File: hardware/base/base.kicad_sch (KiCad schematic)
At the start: 40 parts, among them J1 SWD, J2 USB_B_Mini, J4 Serial Interface, J5 Debug, Q1 Q_NMOS_GSD, SW3 RotaryEncoder_Switch, U1 nRF52833-QDxx, U2 Linear regulator, Y1 32MHz, Y2 32kHz

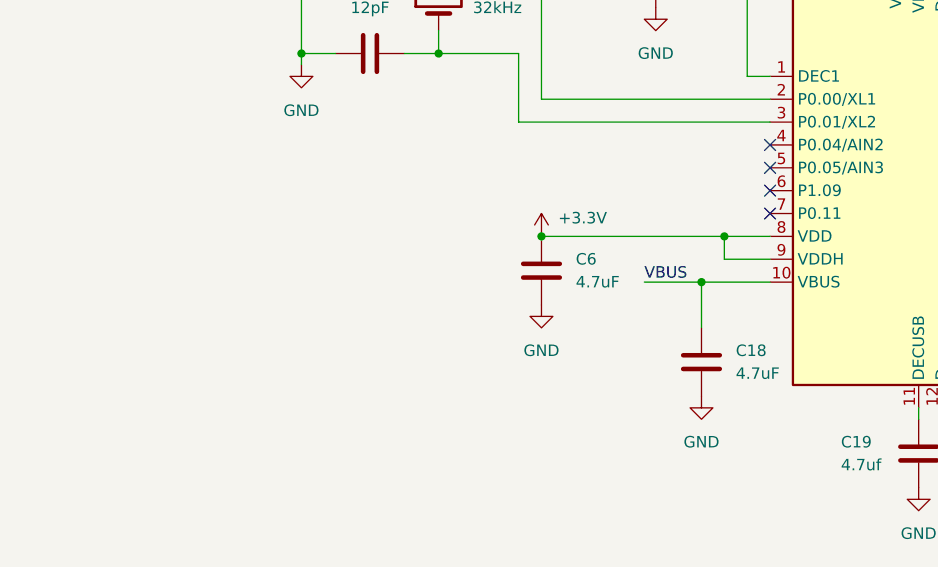
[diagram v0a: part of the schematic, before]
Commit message: add oled display
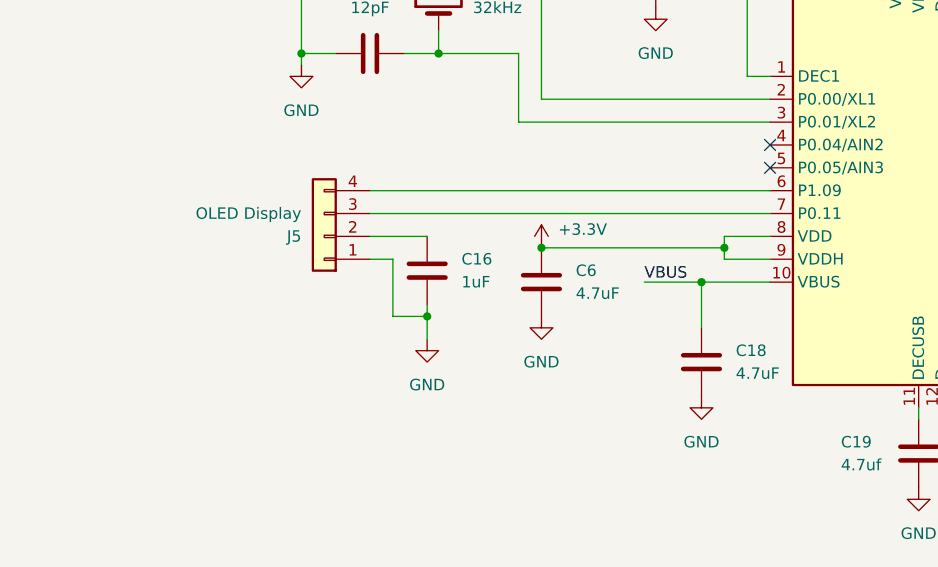
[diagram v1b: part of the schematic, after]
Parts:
- added C16: 1uF, Capacitor_SMD:C_0603_1608Metric, symbol Device:C
- added J5: OLED Display, Connector_PinHeader_2.54mm:PinHeader_1x04_P2.54mm_Vertical, symbol Connector_Generic:Conn_01x04
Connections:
- net GND: now also C16.2, J5.1 (Pin_1)
- net at U1.6 (P1.09): now also J5.4 (Pin_4)
- net at U1.7 (P0.11): now also J5.3 (Pin_3)
- new net: C16.1, J5.2 (Pin_2)
- no-connect marks 11 -> 9
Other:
- moved on the sheet: C6

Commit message: add rotary encoder footprint
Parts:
- SW3: footprint (none) -> Rotary_Encoder:RotaryEncoder_Bourns_Vertical_PEC12R-3x17F-Sxxxx
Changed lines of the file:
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@@
 			)
 		)
-		(property "Footprint" ""
+		(property "Footprint" "Rotary_Encoder:RotaryEncoder_Bourns_Vertical_PEC12R-3x17F-Sxxxx"
 			(at 39.116 35.56 0)
 			(effects

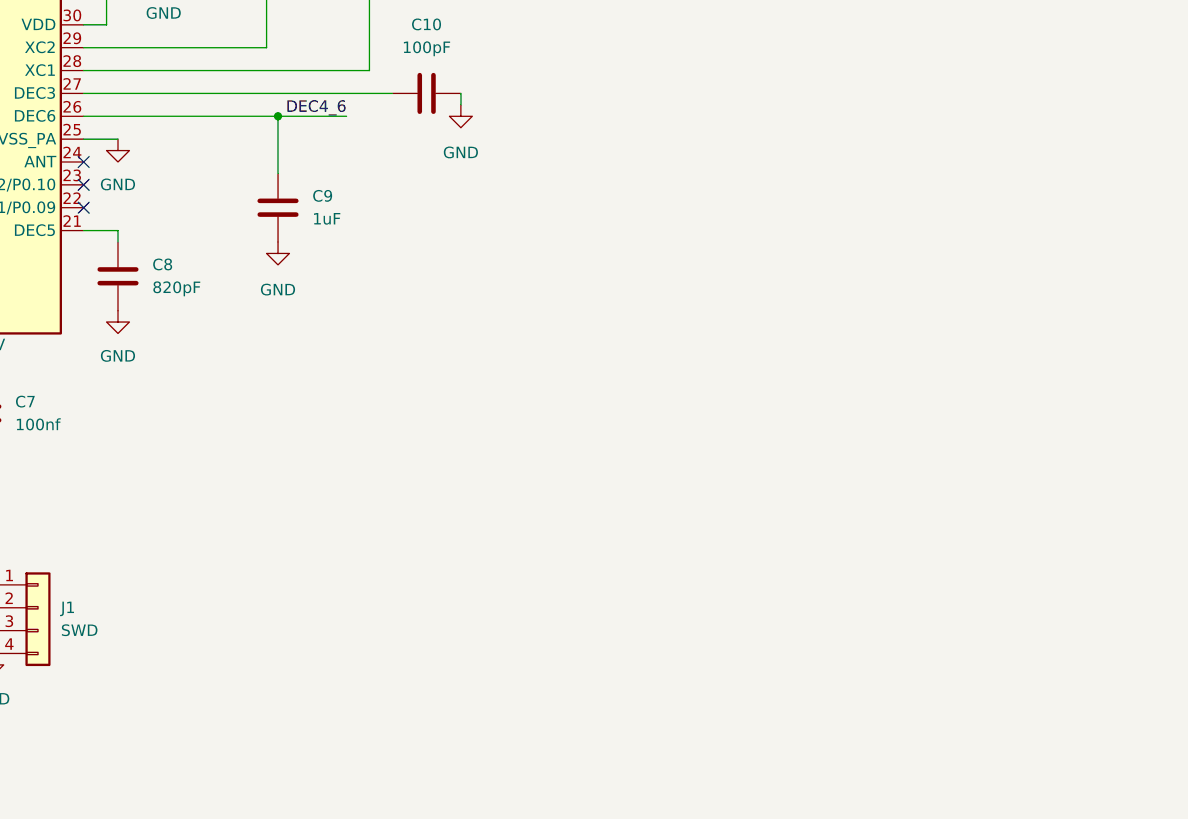
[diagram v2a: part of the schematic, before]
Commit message: add amplifier and speaker symbols
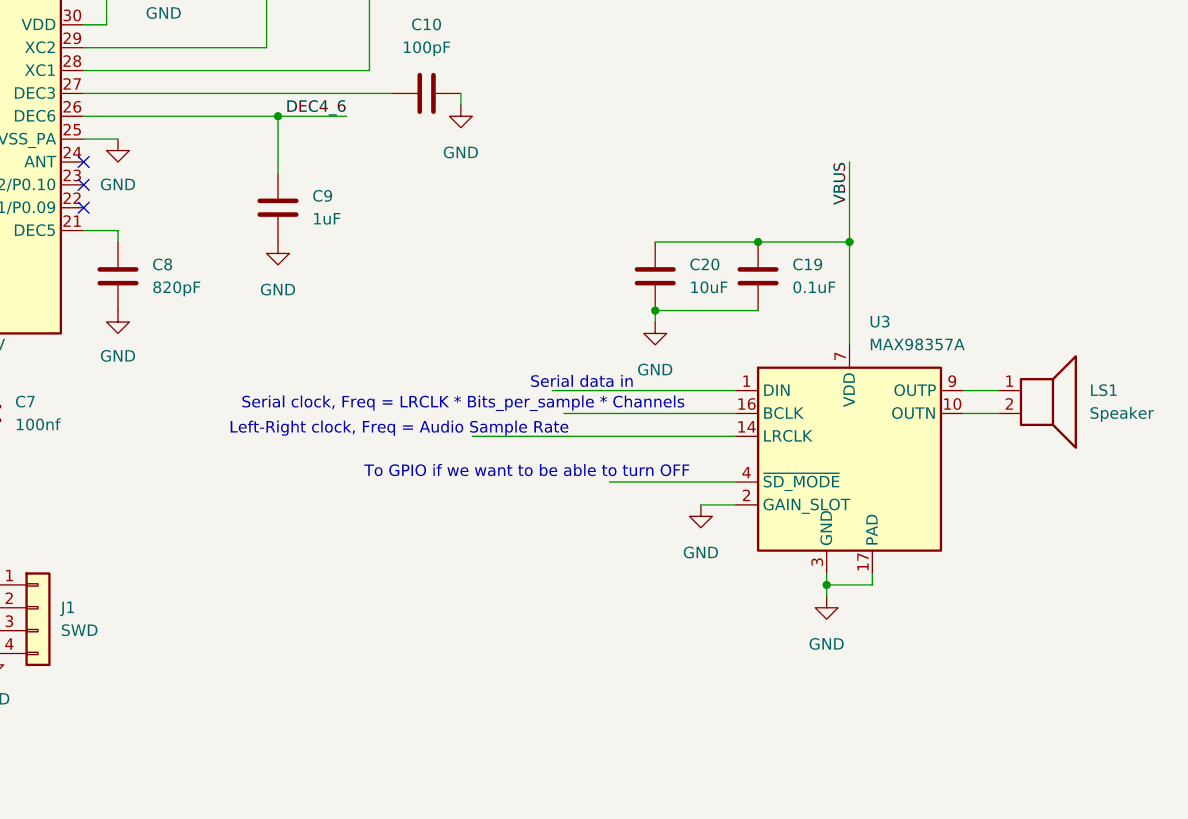
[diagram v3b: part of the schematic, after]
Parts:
- added C19: 0.1uF, Capacitor_SMD:C_0603_1608Metric, symbol Device:C
- added C20: 10uF, Capacitor_SMD:C_0603_1608Metric, symbol Device:C
- added LS1: Speaker, symbol Device:Speaker
- added U3: MAX98357A, Package_DFN_QFN:TQFN-16-1EP_3x3mm_P0.5mm_EP1.23x1.23mm, symbol Audio:MAX98357A
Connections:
- net GND: now also C19.1, C20.1, U3.11 (GND), U3.15 (GND), U3.17 (PAD), U3.2 (GAIN_SLOT), U3.3 (GND)
- net VBUS: now also C19.2, C20.2, U3.7 (VDD), U3.8 (VDD)
- new net: LS1.2, U3.10 (OUTN)
- new net: LS1.1, U3.9 (OUTP)
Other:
- note added: "Left-Right clock, Freq = Audio Sample Rate"
- note added: "Serial clock, Freq = LRCLK * Bits_per_sample * Channels"
- note added: "Serial data in"
- note added: "To GPIO if we want to be able to turn OFF"

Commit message: combine components
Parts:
- removed C14, C17: 1uF, Capacitor_SMD:C_0603_1608Metric, symbol Device:C
- removed U2: Linear regulator, Package_TO_SOT_SMD:SOT-89-3_Handsoldering, symbol Regulator_Linear:MCP1700x-330xxMB
- added B1: HD-EMC1203-LW20-R, HD-EMC1203-LW20-R:PUI_HD-EMC1203-LW20-R, symbol HD-EMC1203-LW20-R:HD-EMC1203-LW20-R
- added BT1: Battery_Cell, symbol Device:Battery_Cell
- added C15, C21: 100 nF, Capacitor_SMD:C_0603_1608Metric, symbol Device:C
- added C23: 0.1 uF, Capacitor_SMD:C_0603_1608Metric, symbol Device:C
- added C24, C25: 1.0 uF, Capacitor_SMD:C_0603_1608Metric, symbol Device:C
- added D2: 1N4001, Diode_THT:D_DO-41_SOD81_P10.16mm_Horizontal, symbol Diode:1N4001
- added D4, D5: D, symbol Device:D
- added J6: Conn_01x02_Pin, symbol Connector:Conn_01x02_Pin
- added L1: 300 uH, Inductor_SMD:L_0603_1608Metric, symbol Device:L
- added M1: Fan_ALT, Connector_PinHeader_2.00mm:PinHeader_1x02_P2.00mm_Vertical, symbol Motor:Fan_ALT
- added Q2, Q3: Q_NMOS_GSD, Package_TO_SOT_SMD:SOT-23, symbol Device:Q_NMOS_GSD
- added Q5: NPN, BJT SMD Transistor (MMBT2222A_DG_215):SOT95P230X110-3N, symbol Simulation_SPICE:NPN
- added R10, R6: 10kOhm, Resistor_SMD:R_0603_1608Metric, symbol Device:R
- added R11, R5, R7: 100 Ohm, Resistor_SMD:R_0603_1608Metric, symbol Device:R
- added R8: 68 kOhm, Resistor_SMD:R_0603_1608Metric, symbol Device:R
- added R9: 132 kOhm, Resistor_SMD:R_0603_1608Metric, symbol Device:R
- added RX1: 664k, Resistor_SMD:R_0603_1608Metric, symbol Device:R
- added RX2: 15, Resistor_SMD:R_0603_1608Metric, symbol Device:R
- added TP3, TP4: TestPoint, E7020E:TestPoint_THTPad_1.5x1.5mm_Drill0.8mm, symbol Connector:TestPoint
- added U4: MCP1700x-330xxMB, Package_TO_SOT_SMD:SOT-89-3_Handsoldering, symbol Regulator_Linear:MCP1700x-330xxMB
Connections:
- net +3.3V: now also B1.P, C23.1, D2.1 (K), D4.1 (K), D5.1 (K)
- net GND: now also BT1.2 (-), C21.2, C24.2, C25.2, J6.1 (Pin_1), Q2.2 (S), Q5.3 (E), R10.2, R11.2, R6.2, R9.2, U4.1 (GND)
- net VBUS: now also C24.1, L1.1, R8.1, RX2.2, U4.2 (VI)
- net at Q1.1 (G), R5.1, TP1.1: now also Q5.2 (B), R6.1, R7.2, TP3.1; no longer U1.32 (AIN0/P0.02)
- net HUMIDIFIER_MOSFET_GATE: now reaches U1.17 (P0.20)
- net HUMIDIFIER_MOSFET_GATE: now also R5.1
- net DETECT_VSOURCE: now reaches U1.22 (NFC1/P0.09)
- net DETECT_VSOURCE: now also R8.2, R9.1
- net at U1.23 (NFC2/P0.10): now also Q2.1 (G), RX1.1
- net AMP_DIN: now reaches U1.36 (AIN7/P0.31)
- net AMP_DIN: now also U3.1 (DIN)
- net AMP_BCLK: now reaches U1.4 (P0.04/AIN2)
- net AMP_BCLK: now also U3.16 (BCLK)
- net AMP_LRCLK: now reaches U1.5 (P0.05/AIN3)
- net AMP_LRCLK: now also U3.14 (LRCLK)
- net at U3.4 (~{SD_MODE}): now also RX1.2
- new net: C25.1, D5.2 (A), U4.3 (VO)
- new net: Q3.1 (G), R10.1, R5.2, TP4.1
- new net: B1.N, C23.2, D2.2 (A), Q5.1 (C)
- new net: C15.2, C21.1, J6.2 (Pin_2)
- new net: BT1.1 (+), D4.2 (A)
- new net: Q3.2 (S), R11.1
- new net: C15.1, L1.2, Q3.3 (D)
- new net: M1.1 (+), Q2.3 (D)
- new net: M1.2 (-), RX2.1
- new net LED_HAPTIC: R7.1, U1.32 (AIN0/P0.02)
- no-connect marks 9 -> 3
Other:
- note added: "3.3/5 = (132)/(68+132)"
- note added: "BCLK, Serial clock, Freq = LRCLK * Bits_per_sample * Channels"
- note added: "DIN = Serial data in"
- note added: "Divide voltage to get 3.3V from 5V"
- note added: "LRCLK, Left-Right clock, Freq = Audio Sample Rate"
- note added: "Operating Voltage Range: 2.5 ~ 3.5 V_{DC}"
- note added: "SDMODE, To GPIO if we want to be able to turn OFF"
- note added: "V_{out}= V_{in} * (R_{2})/(R_{1}+R_{2})"
- note added: "http://www.learningaboutelectronics.com/Articles/Vibration-motor-circuit.php"
- note removed: "Left-Right clock, Freq = Audio Sample Rate"
- note removed: "Serial clock, Freq = LRCLK * Bits_per_sample * Channels"
- note removed: "Serial data in"
- note removed: "To GPIO if we want to be able to turn OFF"
- moved on the sheet: C19, C20, D1, GND1, GND2, GND3, GND4, J5, LS1, Q1, R3, R4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

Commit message: fix error
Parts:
- removed Q5: NPN, BJT SMD Transistor (MMBT2222A_DG_215):SOT95P230X110-3N, symbol Simulation_SPICE:NPN
- removed R5: 10k, Resistor_SMD:R_0603_1608Metric, symbol Device:R
- removed R6: 10kOhm, Resistor_SMD:R_0603_1608Metric, symbol Device:R
- removed RX2: 15, Resistor_SMD:R_0603_1608Metric, symbol Device:R
- removed TP3: TestPoint, E7020E:TestPoint_THTPad_1.5x1.5mm_Drill0.8mm, symbol Connector:TestPoint
- added Q4: MMBT2222A, Package_TO_SOT_SMD:SOT-23, symbol Transistor_BJT:MMBT2222A
- added R2: 10k, Resistor_SMD:R_0603_1608Metric, symbol Device:R
- added TP2: TestPoint, E7020E:TestPoint_THTPad_1.5x1.5mm_Drill0.8mm, symbol Connector:TestPoint
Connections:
- net GND: now also Q4.2 (E), R2.2; no longer U3.17 (PAD)
- net HUMIDIFIER_MOSFET_GATE: now also Q3.1 (G), R10.1, R5.2, TP4.1
- net LED_HAPTIC: now also TP1.1
- net VBUS: now also M1.2 (-)
- net at B1.N, C23.2, D2.2 (A): now also Q4.3 (C)
- net at Q1.1 (G), R7.2: now also Q4.1 (B), R2.1; no longer TP1.1
- net at Q2.1 (G), RX1.1, U1.23 (NFC2/P0.10): now also TP2.1
- no-connect marks 3 -> 4
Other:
- note added: "Exposed Pad. The exposed pad is not internally connected. Connect the exposed page to a solid ground plane for thermal dissipation."
- moved on the sheet: R5, R7, TP1
